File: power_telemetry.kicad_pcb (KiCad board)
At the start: 2 copper layers, 86.5 x 49 mm, 49 parts, among them J1 Screw_Terminal_1x02, J10 CONN_01X04, J11 CONN_01X04, J12 GS2, J2 CONN_01X02, J3 CONN_01X03, J4 CONN_01X02, J5 CONN_01X02, J6 CONN_01X03, J7 CONN_01X02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

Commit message: fixed order of power supplies
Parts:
- moved J8 32.0 mm to (126.0, 71.0)
- moved J3 16.0 mm to (94.0, 71.0)
- moved J6 16.0 mm to (110.0, 71.0)
- moved G*** 5.00 mm to (136.5, 95.0)
- moved REF*** 2.55 mm to (106.2, 94.8)
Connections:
- C6 pad 2: VCC -> /VCCB
- C7 pad 2: VCC -> /VCCB
- C8 pad 2: VCC -> /VCCA
- C9 pad 1: VCC -> /VCCA
- J3 pad 3: VCC -> /VCCB
- J4 pad 2: VCC -> /VCCB
- J6 pad 3: VCC -> /VCCA
- J7 pad 2: VCC -> /VCCA
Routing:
- net VCC: track 178.3 -> 145.9 mm
- net /VCCB: track 0.00 -> 16.2 mm
- net /VCCA: track 0.00 -> 16.2 mm
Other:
- board text added: "Power/Telemetry/ Fans Rev A"

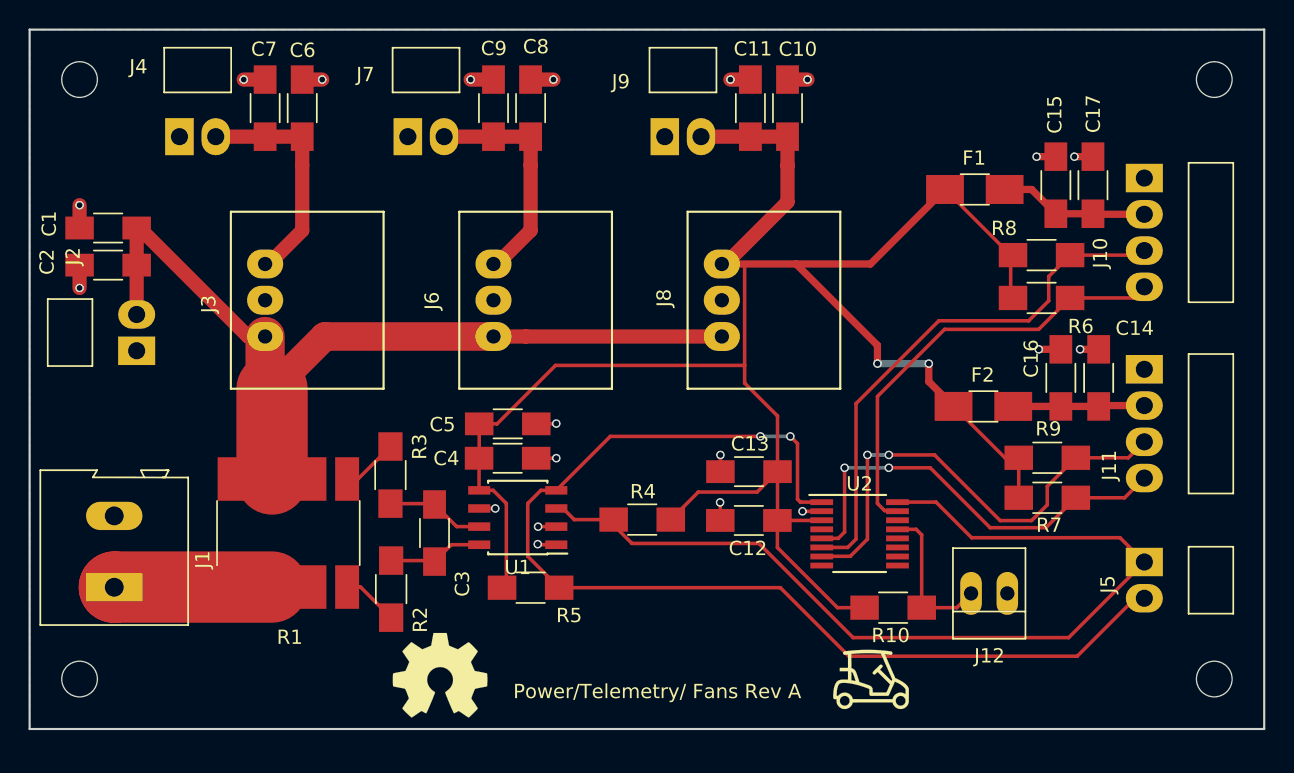
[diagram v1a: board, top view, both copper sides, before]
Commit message: now using correctly sized shunt resistor
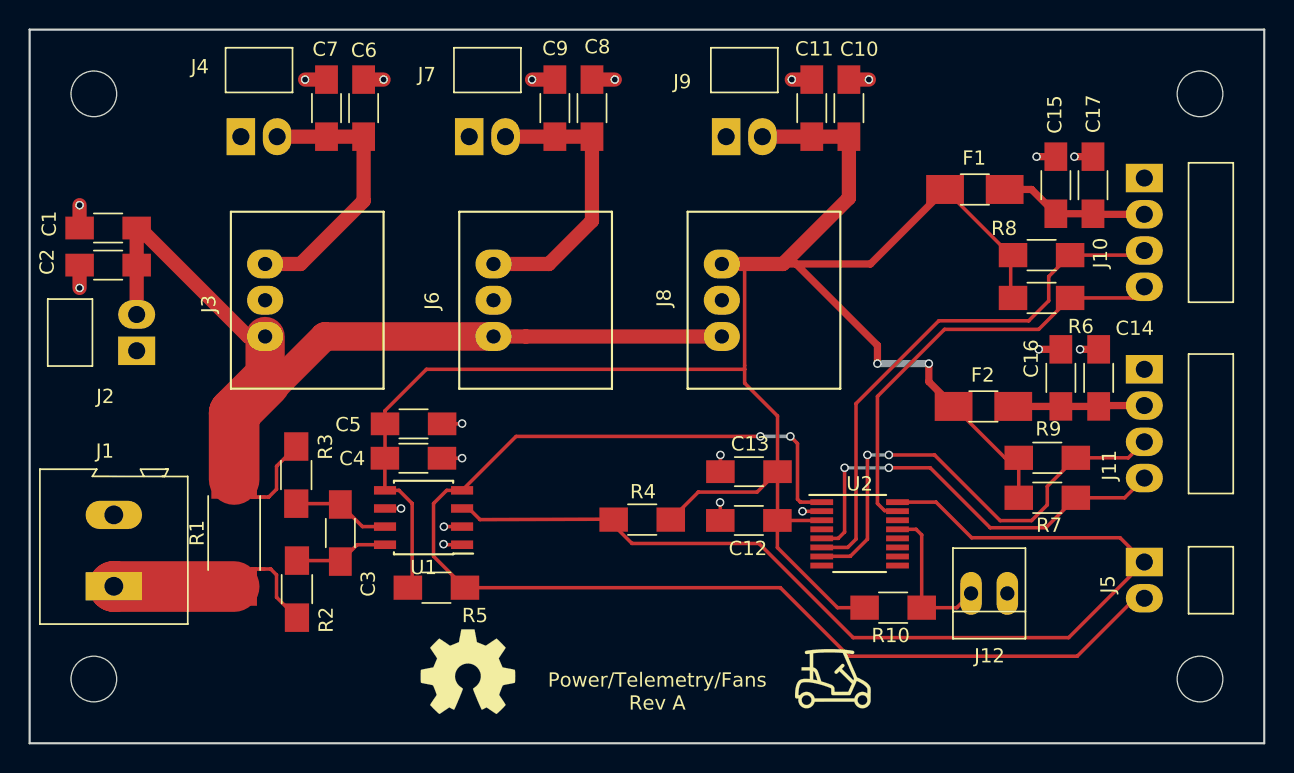
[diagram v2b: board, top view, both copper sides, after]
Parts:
- R1: value .05k -> 6.5 mOhms; footprint lib_fp:R_3637_HandSoldering -> lib_fp:R_2512_Kelvin_HandSoldering
- REF** (x4): value MountingHole_2.5mm -> MountingHole_3.2mm; footprint Mounting_Holes:MountingHole_2.5mm -> Mounting_Holes:MountingHole_3.2mm_M3
- moved C3 6.60 mm to (99.3, 84.8)
- moved U1 6.60 mm to (105.1, 83.7)
- moved C4 6.60 mm to (104.4, 79.5)
- moved C5 6.60 mm to (104.4, 77.1)
- moved R2 6.60 mm to (96.2, 88.7)
- moved R3 6.60 mm to (96.2, 80.7)
- moved R5 6.60 mm to (106.0, 88.6)
- moved C10 4.30 mm to (134.9, 55.0)
- moved C11 4.30 mm to (132.3, 55.0)
- moved C6 4.30 mm to (100.9, 55.0)
- moved C8 4.30 mm to (116.9, 55.0)
- moved C7 4.30 mm to (98.3, 55.0)
- moved C9 4.30 mm to (114.3, 55.0)
- moved J4 4.30 mm to (92.3, 57.0)
- moved J7 4.30 mm to (108.3, 57.0)
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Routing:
- net /SCL: track 78.2 -> 91.4 mm
- net VCC: track 145.9 -> 157.3 mm
- net /SDA: track 66.4 -> 73.0 mm
- net /VCCA: track 16.2 -> 20.4 mm
- net /VCCB: track 16.2 -> 19.3 mm
- net +12V: track 65.5 -> 68.0 mm
- net Net-(J1-Pad1): track 15.0 -> 13.5 mm
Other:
- board size 86.5 x 49 mm -> 86.5 x 50 mm
- board text added: "Power/Telemetry/Fans Rev A"
- board text removed: "Power/Telemetry/ Fans Rev A"
